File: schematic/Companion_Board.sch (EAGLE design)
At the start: 47 parts, among them Q1 16MHz

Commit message: Some corrections to layout.
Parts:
- renumbered TP2 to I2C_DAT, TP3 to I2C_CLK
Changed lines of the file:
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@@
 <grid distance="0.1" unitdist="inch" unit="inch" style="lines" multiple="1" display="no" altdistance="0.01" altunitdist="inch" altunit="inch"/>
 <layers>
-<layer number="1" name="Top" color="4" fill="1" visible="yes" active="no"/>
-<layer number="16" name="Bottom" color="1" fill="1" visible="yes" active="no"/>
-<layer number="17" name="Pads" color="2" fill="1" visible="yes" active="no"/>
-<layer number="18" name="Vias" color="2" fill="1" visible="yes" active="no"/>
-<layer number="19" name="Unrouted" color="6" fill="1" visible="yes" active="no"/>
-<layer number="20" name="Dimension" color="15" fill="1" visible="yes" active="no"/>
-<layer number="21" name="tPlace" color="7" fill="1" visible="yes" active="no"/>
-<layer number="22" name="bPlace" color="7" fill="1" visible="yes" active="no"/>
-<layer number="23" name="tOrigins" color="15" fill="1" visible="yes" active="no"/>
-<layer number="24" name="bOrigins" color="15" fill="1" visible="yes" active="no"/>
-<layer number="25" name="tNames" color="7" fill="1" visible="yes" active="no"/>
-<layer number="26" name="bNames" color="7" fill="1" visible="yes" active="no"/>
-<layer number="27" name="tValues" color="7" fill="1" visible="yes" active="no"/>
-<layer number="28" name="bValues" color="7" fill="1" visible="yes" active="no"/>
+<layer number="1" name="Top" color="4" fill="1" visible="no" active="no"/>
+<layer number="16" name="Bottom" color="1" fill="1" visible="no" active="no"/>
+<layer number="17" name="Pads" color="2" fill="1" visible="no" active="no"/>
+<layer number="18" name="Vias" color="2" fill="1" visible="no" active="no"/>
+<layer number="19" name="Unrouted" color="6" fill="1" visible="no" active="no"/>
+<layer number="20" name="Dimension" color="15" fill="1" visible="no" active="no"/>
+<layer number="21" name="tPlace" color="7" fill="1" visible="no" active="no"/>
+<layer number="22" name="bPlace" color="7" fill="1" visible="no" active="no"/>
+<layer number="23" name="tOrigins" color="15" fill="1" visible="no" active="no"/>
+<layer number="24" name="bOrigins" color="15" fill="1" visible="no" active="no"/>
+<layer number="25" name="tNames" color="7" fill="1" visible="no" active="no"/>
+<layer number="26" name="bNames" color="7" fill="1" visible="no" active="no"/>
+<layer number="27" name="tValues" color="7" fill="1" visible="no" active="no"/>
+<layer number="28" name="bValues" color="7" fill="1" visible="no" active="no"/>
 <layer number="29" name="tStop" color="7" fill="3" visible="no" active="no"/>
 <layer number="30" name="bStop" color="7" fill="6" visible="no" active="no"/>
@@
 <layer number="35" name="tGlue" color="7" fill="4" visible="no" active="no"/>
 <layer number="36" name="bGlue" color="7" fill="5" visible="no" active="no"/>
-<layer number="37" name="tTest" color="7" fill="1" visible="yes" active="no"/>
-<layer number="38" name="bTest" color="7" fill="1" visible="yes" active="no"/>
+<layer number="37" name="tTest" color="7" fill="1" visible="no" active="no"/>
+<layer number="38" name="bTest" color="7" fill="1" visible="no" active="no"/>
 <layer number="39" name="tKeepout" color="4" fill="11" visible="no" active="no"/>
 <layer number="40" name="bKeepout" color="1" fill="11" visible="no" active="no"/>
@@
 <layer number="44" name="Drills" color="7" fill="1" visible="no" active="no"/>
 <layer number="45" name="Holes" color="7" fill="1" visible="no" active="no"/>
-<layer number="46" name="Milling" color="3" fill="1" visible="yes" active="no"/>
-<layer number="47" name="Measures" color="7" fill="1" visible="yes" active="no"/>
-<layer number="48" name="Document" color="7" fill="1" visible="yes" active="no"/>
-<layer number="49" name="Reference" color="7" fill="1" visible="yes" active="no"/>
-<layer number="50" name="dxf" color="7" fill="1" visible="yes" active="no"/>
-<layer number="51" name="tDocu" color="7" fill="1" visible="yes" active="no"/>
-<layer number="52" name="bDocu" color="7" fill="1" visible="yes" active="no"/>
-<layer number="53" name="tGND_GNDA" color="7" fill="9" visible="yes" active="no"/>
-<layer number="54" name="bGND_GNDA" color="1" fill="9" visible="yes" active="no"/>
-<layer number="56" name="wert" color="7" fill="1" visible="yes" active="no"/>
-<layer number="57" name="tCAD" color="7" fill="1" visible="yes" active="no"/>
-<layer number="59" name="tCarbon" color="7" fill="1" visible="yes" active="no"/>
-<layer number="60" name="bCarbon" color="7" fill="1" visible="yes" active="no"/>
+<layer number="46" name="Milling" color="3" fill="1" visible="no" active="no"/>
+<layer number="47" name="Measures" color="7" fill="1" visible="no" active="no"/>
+<layer number="48" name="Document" color="7" fill="1" visible="no" active="no"/>
+<layer number="49" name="Reference" color="7" fill="1" visible="no" active="no"/>
+<layer number="50" name="dxf" color="7" fill="1" visible="no" active="no"/>
+<layer number="51" name="tDocu" color="7" fill="1" visible="no" active="no"/>
+<layer number="52" name="bDocu" color="7" fill="1" visible="no" active="no"/>
+<layer number="53" name="tGND_GNDA" color="7" fill="9" visible="no" active="no"/>
+<layer number="54" name="bGND_GNDA" color="1" fill="9" visible="no" active="no"/>
+<layer number="56" name="wert" color="7" fill="1" visible="no" active="no"/>
+<layer number="57" name="tCAD" color="7" fill="1" visible="no" active="no"/>
+<layer number="59" name="tCarbon" color="7" fill="1" visible="no" active="no"/>
+<layer number="60" name="bCarbon" color="7" fill="1" visible="no" active="no"/>
 <layer number="90" name="Modules" color="5" fill="1" visible="yes" active="yes"/>
 <layer number="91" name="Nets" color="2" fill="1" visible="yes" active="yes"/>
@@
 <part name="C4" library="resistor" deviceset="C-EU" device="C0805" value="6.8pF"/>
 <part name="TP1" library="testpad" deviceset="TP" device="PAD1-13"/>
-<part name="TP2" library="testpad" deviceset="TP" device="PAD1-13"/>
-<part name="TP3" library="testpad" deviceset="TP" device="PAD1-13"/>
+<part name="I2C_DAT" library="testpad" deviceset="TP" device="PAD1-13"/>
+<part name="I2C_CLK" library="testpad" deviceset="TP" device="PAD1-13"/>
 <part name="JP12" library="pinhead" deviceset="PINHD-1X3" device="/90" value="PWM Light Control"/>
 <part name="SUPPLY15" library="supply2" deviceset="GND" device=""/>
@@
 <instance part="C4" gate="G$1" x="375.92" y="104.14"/>
 <instance part="TP1" gate="G$1" x="129.54" y="152.4"/>
-<instance part="TP2" gate="G$1" x="302.26" y="175.26"/>
-<instance part="TP3" gate="G$1" x="307.34" y="175.26"/>
+<instance part="I2C_DAT" gate="G$1" x="302.26" y="175.26"/>
+<instance part="I2C_CLK" gate="G$1" x="307.34" y="175.26"/>
 <instance part="JP12" gate="A" x="398.78" y="132.08"/>
 <instance part="SUPPLY15" gate="GND" x="383.54" y="124.46"/>
@@
 <label x="279.4" y="167.64" size="1.778" layer="95"/>
 <pinref part="U$1" gate="G$1" pin="P1.2/UCB0SIMO/UCB0SDA/TB0TRG/OA0-/A2/VEREF-"/>
-<pinref part="TP2" gate="G$1" pin="TP"/>
+<pinref part="I2C_DAT" gate="G$1" pin="TP"/>
 <wire x1="302.26" y1="167.64" x2="302.26" y2="172.72" width="0.1524" layer="91"/>
 <wire x1="302.26" y1="167.64" x2="332.74" y2="167.64" width="0.1524" layer="91"/>
@@
 <label x="279.4" y="165.1" size="1.778" layer="95"/>
 <pinref part="U$1" gate="G$1" pin="P1.3/UCB0SOMI/UCB0SCL/OA0O/A3"/>
-<pinref part="TP3" gate="G$1" pin="TP"/>
+<pinref part="I2C_CLK" gate="G$1" pin="TP"/>
 <wire x1="307.34" y1="165.1" x2="307.34" y2="172.72" width="0.1524" layer="91"/>
 <label x="347.98" y="165.1" size="1.778" layer="95"/>

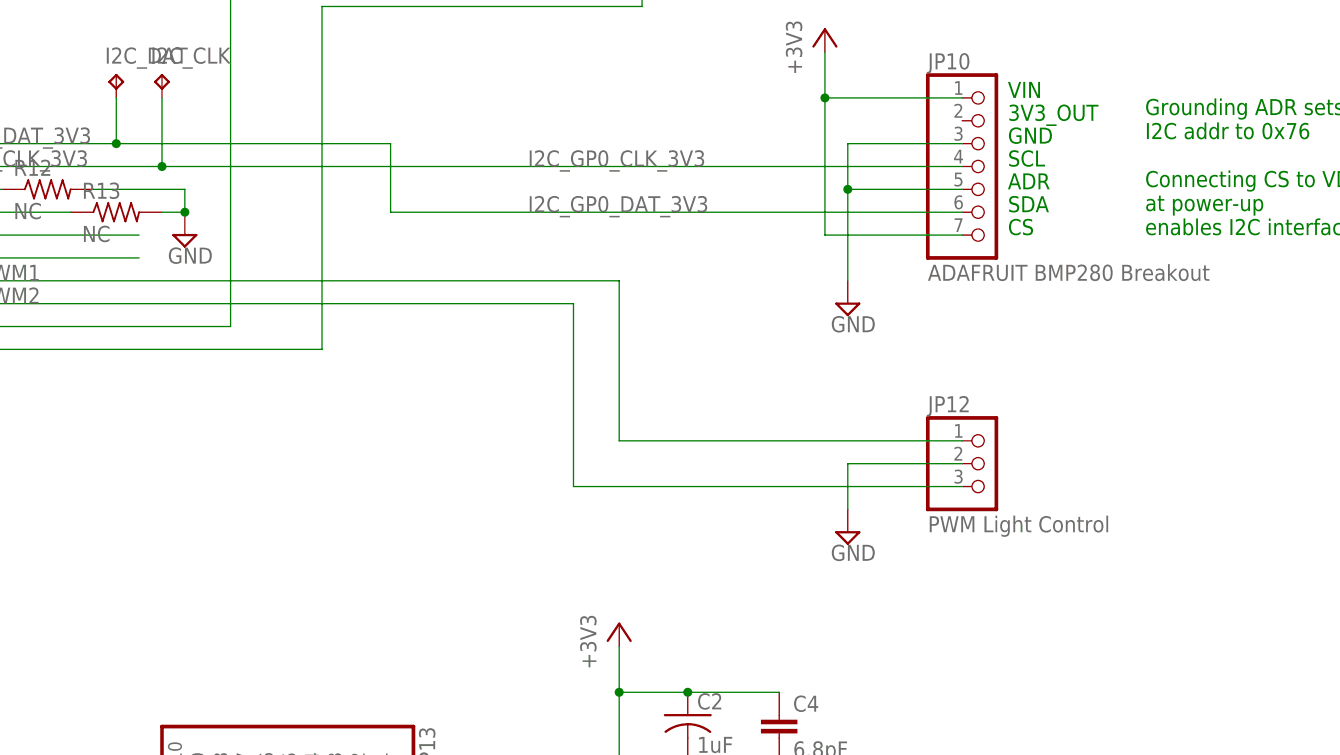
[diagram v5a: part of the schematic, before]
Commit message: Pre-production iteration on companion board, including BOM.
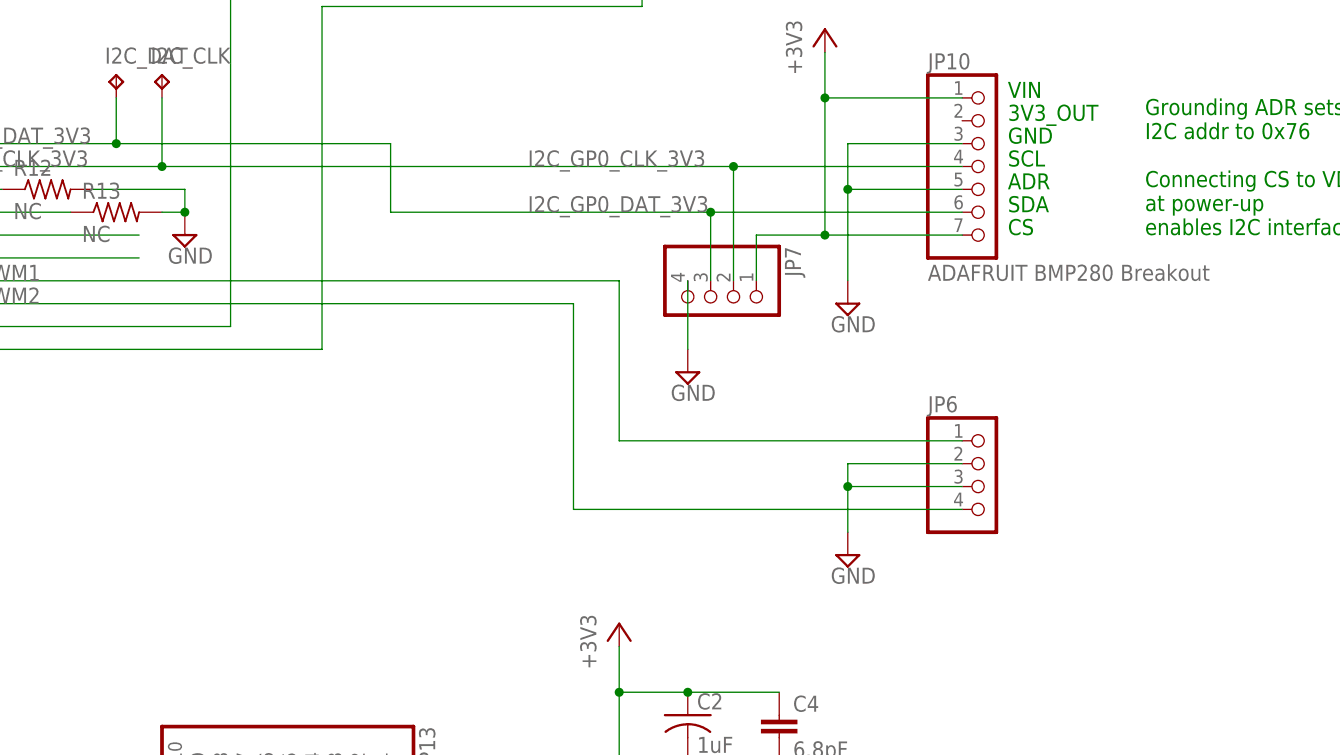
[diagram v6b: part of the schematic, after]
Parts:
- removed JP12: PWM Light Control, pinhead:PINHD-1X3/90
- added JP6: (no value), pinhead:PINHD-1X4/90
- added JP7: (no value), pinhead:PINHD-1X4
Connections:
- net +3V3: now also JP7.1
- net GND: now also JP6.2, JP6.3, JP7.4; no longer JP12.2
- net I2C_GP0_CLK_3V3: now also JP7.2
- net I2C_GP0_DAT_3V3: now also JP7.3
- net LIGHT_PWM1: now also JP6.1; no longer JP12.1
- net LIGHT_PWM2: now also JP6.4; no longer JP12.3
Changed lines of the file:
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@@
 <part name="I2C_DAT" library="testpad" deviceset="TP" device="PAD1-13"/>
 <part name="I2C_CLK" library="testpad" deviceset="TP" device="PAD1-13"/>
-<part name="JP12" library="pinhead" deviceset="PINHD-1X3" device="/90" value="PWM Light Control"/>
 <part name="SUPPLY15" library="supply2" deviceset="GND" device=""/>
 <part name="JP13" library="pinhead" deviceset="PINHD-1X10" device=""/>
@@
 <part name="SUPPLY24" library="supply2" deviceset="GND" device=""/>
 <part name="U$3" library="companion_board" deviceset="2N7002DW" device=""/>
+<part name="JP6" library="pinhead" deviceset="PINHD-1X4" device="/90"/>
+<part name="JP7" library="pinhead" deviceset="PINHD-1X4" device=""/>
+<part name="SUPPLY1" library="supply2" deviceset="GND" device=""/>
 </parts>
 <sheets>
@@
 <instance part="I2C_DAT" gate="G$1" x="302.26" y="175.26"/>
 <instance part="I2C_CLK" gate="G$1" x="307.34" y="175.26"/>
-<instance part="JP12" gate="A" x="398.78" y="132.08"/>
-<instance part="SUPPLY15" gate="GND" x="383.54" y="124.46"/>
+<instance part="SUPPLY15" gate="GND" x="383.54" y="121.92"/>
 <instance part="JP13" gate="A" x="322.58" y="96.52" rot="R270"/>
 <instance part="JP14" gate="A" x="320.04" y="17.78" rot="R270"/>
@@
 <instance part="U$3" gate="G$1" x="119.38" y="116.84" rot="MR0"/>
 <instance part="U$3" gate="G$2" x="71.12" y="116.84" rot="MR0"/>
+<instance part="JP6" gate="A" x="398.78" y="129.54"/>
+<instance part="JP7" gate="A" x="368.3" y="149.86" rot="R270"/>
+<instance part="SUPPLY1" gate="GND" x="365.76" y="142.24"/>
 </instances>
 <busses>
@@
 <segment>
 <pinref part="SUPPLY15" gate="GND" pin="GND"/>
-<pinref part="JP12" gate="A" pin="2"/>
-<wire x1="383.54" y1="127" x2="383.54" y2="132.08" width="0.1524" layer="91"/>
+<wire x1="383.54" y1="124.46" x2="383.54" y2="129.54" width="0.1524" layer="91"/>
+<wire x1="383.54" y1="129.54" x2="383.54" y2="132.08" width="0.1524" layer="91"/>
 <wire x1="383.54" y1="132.08" x2="396.24" y2="132.08" width="0.1524" layer="91"/>
+<pinref part="JP6" gate="A" pin="2"/>
+<pinref part="JP6" gate="A" pin="3"/>
+<wire x1="396.24" y1="129.54" x2="383.54" y2="129.54" width="0.1524" layer="91"/>
+<junction x="383.54" y="129.54"/>
 </segment>
 <segment>
@@
 <wire x1="147.32" y1="152.4" x2="149.86" y2="152.4" width="0.1524" layer="91"/>
 <junction x="147.32" y="142.24"/>
+</segment>
+<segment>
+<pinref part="SUPPLY1" gate="GND" pin="GND"/>
+<pinref part="JP7" gate="A" pin="4"/>
+<wire x1="365.76" y1="144.78" x2="365.76" y2="152.4" width="0.1524" layer="91"/>
 </segment>
 </net>
@@
 <wire x1="396.24" y1="172.72" x2="381" y2="172.72" width="0.1524" layer="91"/>
 <junction x="381" y="172.72"/>
+<pinref part="JP7" gate="A" pin="1"/>
+<wire x1="381" y1="157.48" x2="373.38" y2="157.48" width="0.1524" layer="91"/>
+<wire x1="373.38" y1="157.48" x2="373.38" y2="152.4" width="0.1524" layer="91"/>
+<junction x="381" y="157.48"/>
 </segment>
 <segment>
@@
 <wire x1="332.74" y1="167.64" x2="332.74" y2="160.02" width="0.1524" layer="91"/>
 <pinref part="JP10" gate="A" pin="6"/>
-<wire x1="396.24" y1="160.02" x2="332.74" y2="160.02" width="0.1524" layer="91"/>
+<wire x1="396.24" y1="160.02" x2="368.3" y2="160.02" width="0.1524" layer="91"/>
 <label x="347.98" y="160.02" size="1.778" layer="95"/>
+<pinref part="JP7" gate="A" pin="3"/>
+<wire x1="368.3" y1="160.02" x2="332.74" y2="160.02" width="0.1524" layer="91"/>
+<wire x1="368.3" y1="152.4" x2="368.3" y2="160.02" width="0.1524" layer="91"/>
+<junction x="368.3" y="160.02"/>
 </segment>
 </net>
@@
 <label x="347.98" y="165.1" size="1.778" layer="95"/>
 <pinref part="JP10" gate="A" pin="4"/>
-<wire x1="396.24" y1="165.1" x2="307.34" y2="165.1" width="0.1524" layer="91"/>
+<wire x1="396.24" y1="165.1" x2="370.84" y2="165.1" width="0.1524" layer="91"/>
 <junction x="307.34" y="165.1"/>
+<pinref part="JP7" gate="A" pin="2"/>
+<wire x1="370.84" y1="165.1" x2="307.34" y2="165.1" width="0.1524" layer="91"/>
+<wire x1="370.84" y1="152.4" x2="370.84" y2="165.1" width="0.1524" layer="91"/>
+<junction x="370.84" y="165.1"/>
 </segment>
 </net>
@@
 <wire x1="276.86" y1="152.4" x2="358.14" y2="152.4" width="0.1524" layer="91"/>
 <wire x1="358.14" y1="152.4" x2="358.14" y2="134.62" width="0.1524" layer="91"/>
-<pinref part="JP12" gate="A" pin="1"/>
 <wire x1="358.14" y1="134.62" x2="396.24" y2="134.62" width="0.1524" layer="91"/>
+<pinref part="JP6" gate="A" pin="1"/>
 </segment>
 </net>
@@
 <pinref part="U$1" gate="G$1" pin="P2.1/TB1.2"/>
 <label x="279.4" y="149.86" size="1.778" layer="95"/>
-<pinref part="JP12" gate="A" pin="3"/>
-<wire x1="396.24" y1="129.54" x2="353.06" y2="129.54" width="0.1524" layer="91"/>
-<wire x1="353.06" y1="129.54" x2="353.06" y2="149.86" width="0.1524" layer="91"/>
+<wire x1="396.24" y1="127" x2="353.06" y2="127" width="0.1524" layer="91"/>
+<wire x1="353.06" y1="127" x2="353.06" y2="149.86" width="0.1524" layer="91"/>
 <wire x1="353.06" y1="149.86" x2="276.86" y2="149.86" width="0.1524" layer="91"/>
-</segment>
-</net>
+<pinref part="JP6" gate="A" pin="4"/>
+</segment>
+</net>

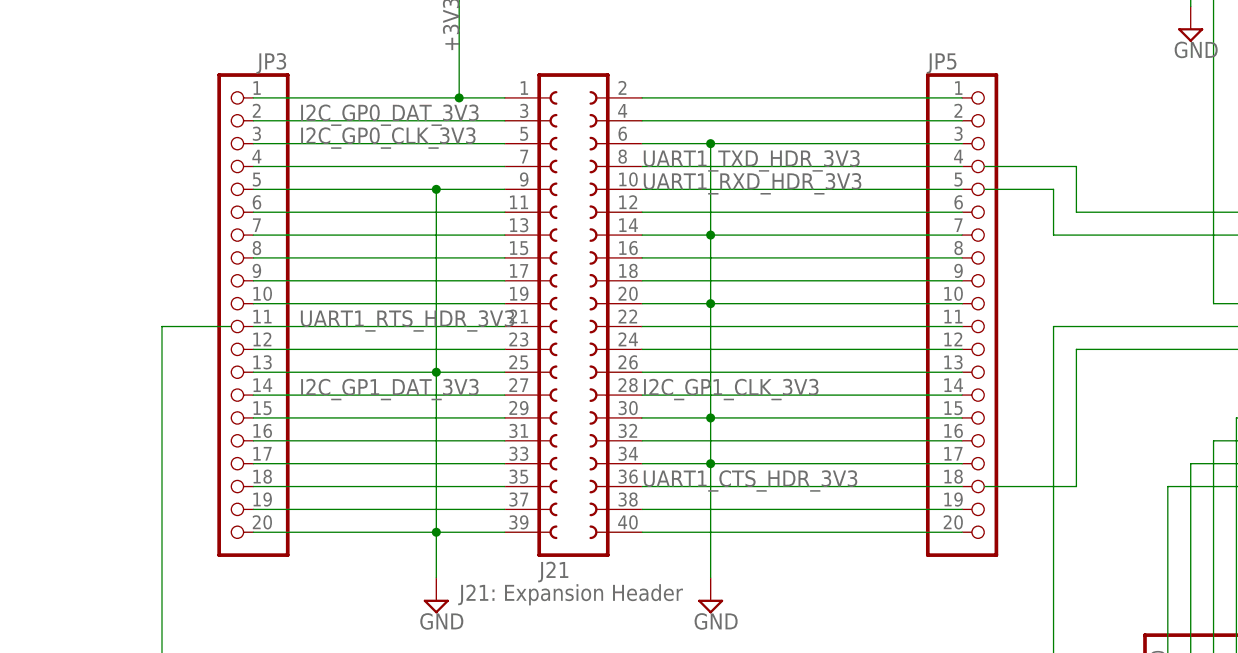
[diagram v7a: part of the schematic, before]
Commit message: Updated schematic with missin serial comms traces to XBee and generated finalized Gerbers.
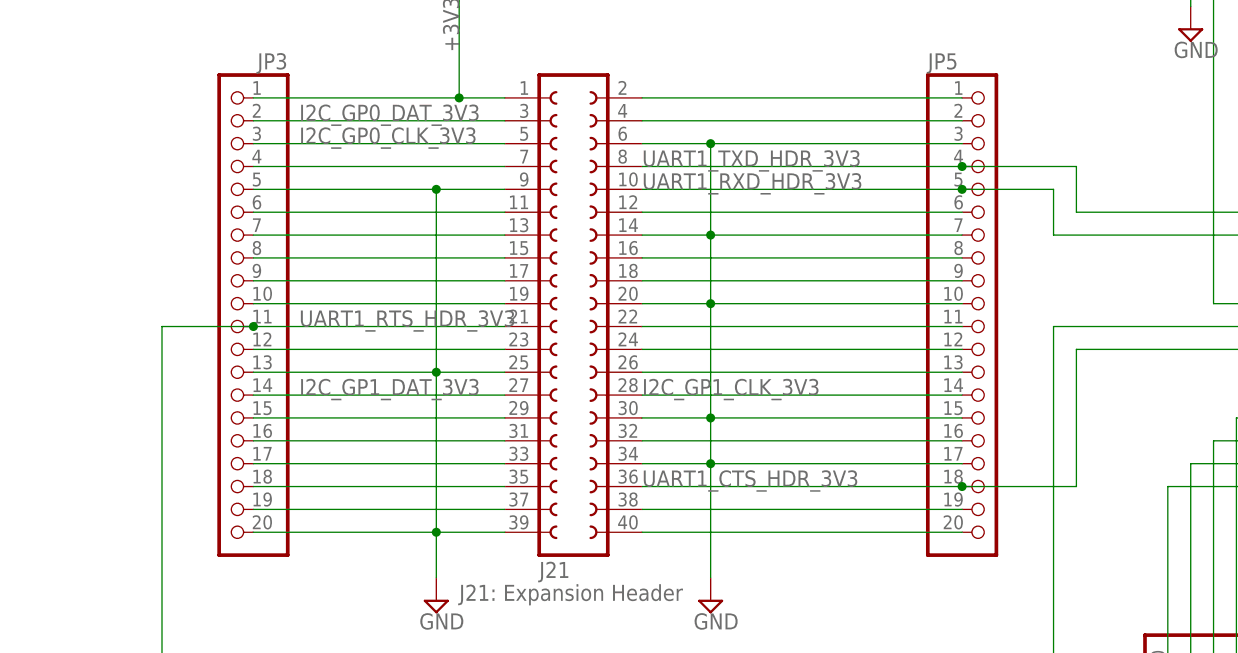
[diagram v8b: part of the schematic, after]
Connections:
- removed net N$11: JP13.3, XB1.DIN/!CONFIG
- removed net N$32: JP14.6, XB1.!RTS!/AD6/DIO6
- removed net N$40: JP14.2, XB1.!CTS!/DIO7
- removed net N$6: JP13.2, XB1.DOUT
- net UART1_CTS_HDR_3V3: now also JP14.6, XB1.!RTS!/AD6/DIO6
- net UART1_RTS_HDR_3V3: now also JP14.2, XB1.!CTS!/DIO7
- net UART1_RXD_HDR_3V3: now also JP13.2, XB1.DOUT
- net UART1_TXD_HDR_3V3: now also JP13.3, XB1.DIN/!CONFIG
